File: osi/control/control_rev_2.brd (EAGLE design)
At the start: 25.4 x 25.4 mm, 15 parts, among them U1 ATMEGA168, Y1 RESONATORSMD

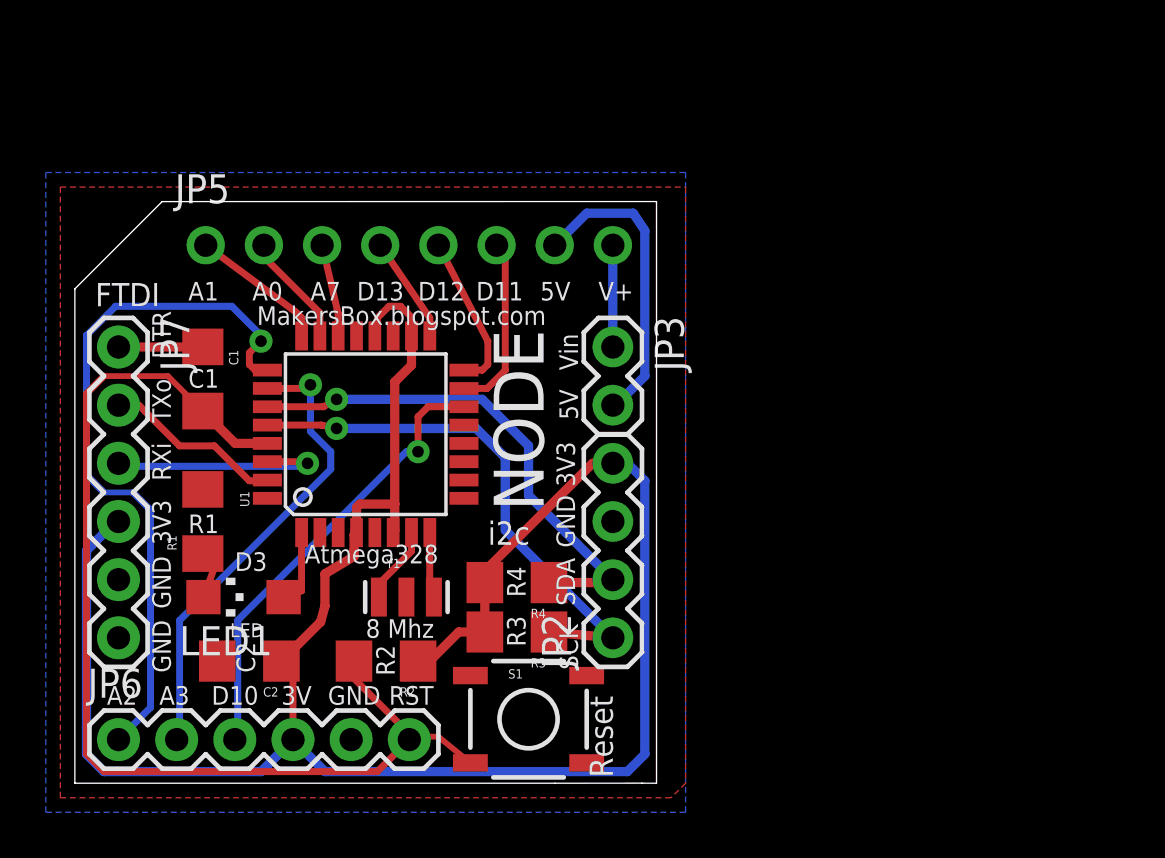
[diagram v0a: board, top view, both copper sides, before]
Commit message: 328p surface mount
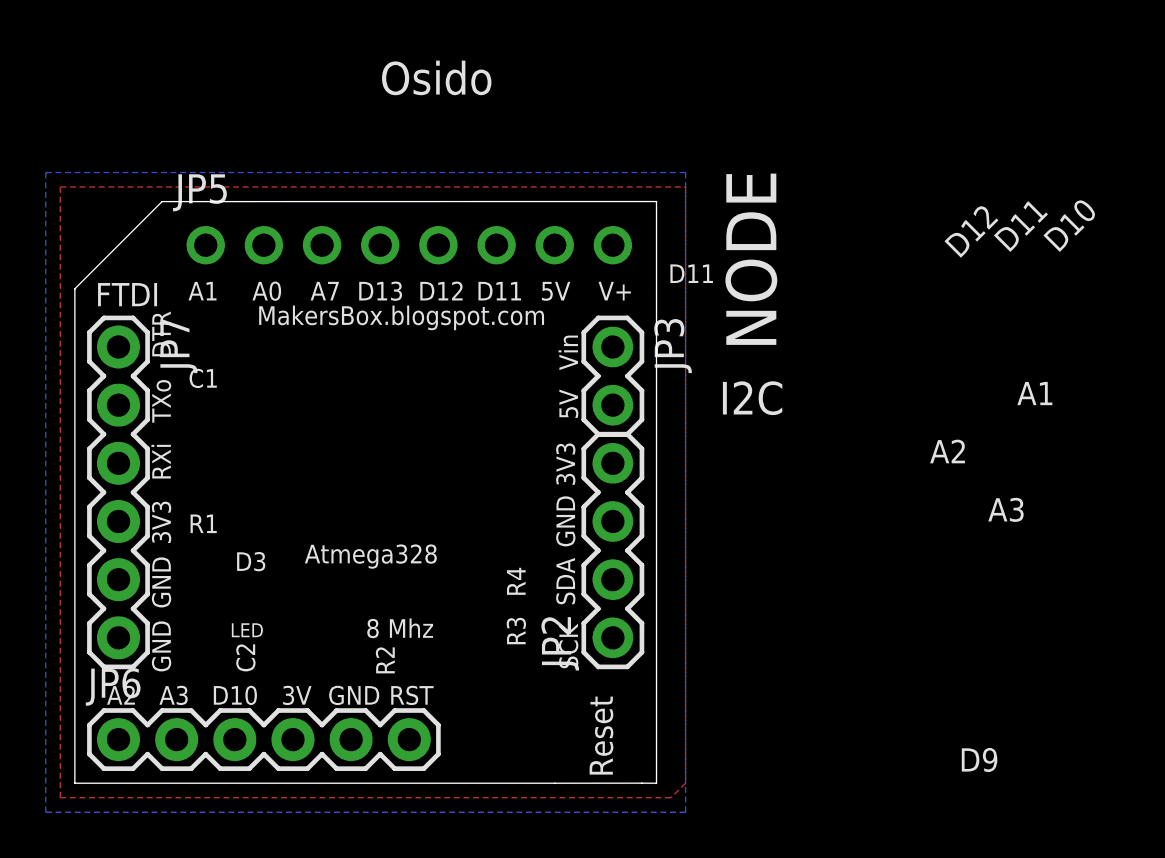
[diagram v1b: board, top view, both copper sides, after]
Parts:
- removed C1, C2, R1, R2, R3, R4: (no value), SparkFun:1206
- removed LED1: (no value), adafruit:CHIPLED_1206
- removed S1: (no value), SparkFun:TACTILE_SWITCH_SMD
- removed U1: ATMEGA168, SparkFun:TQFP32-08
- removed Y1: RESONATORSMD, SparkFun:RESONATOR-SMD
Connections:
- removed net A0: JP5.2, U1.23
- removed net A1: JP5.1, U1.24
- removed net A6: U1.19
- removed net D2: U1.32
- removed net D3: LED1.A, U1.1
- removed net D4: U1.2
- removed net D5: U1.9
- removed net D6: U1.10
- removed net D7: U1.11
- removed net D8: U1.12
- removed net D9: U1.13
- removed net N$1: U1.8, Y1.3
- removed net N$3: U1.7, Y1.1
- removed net N$4: LED1.C, R1.1
- net +3V3: no longer C2.1, R2.1, R3.2, R4.2, U1.18, U1.20, U1.4, U1.6
- net A2: no longer U1.25
- net A3: no longer U1.26
- net A7: no longer U1.22
- net D10: no longer U1.14
- net D11: no longer U1.15
- net D12: no longer U1.16
- net D13: no longer U1.17
- net DTR: no longer C1.1
- net GND: no longer C2.2, R1.2, S1.2, U1.21, U1.3, U1.5, Y1.2
- net RESET: no longer C1.2, R2.2, S1.3, U1.29
- net RXI: no longer U1.30
- net SCL_A5: no longer R3.1, U1.28
- net SDA_A4: no longer R4.1, U1.27
- net TXO: no longer U1.31
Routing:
- net +3V3: track 92.1 -> 0.00 mm
- net RESET: track 47.1 -> 0.00 mm
- net A2: track 31.2 -> 0.00 mm, vias 1 -> 0
- net SCL_A5: track 23.6 -> 0.00 mm, vias 1 -> 0
- net SDA_A4: track 22.5 -> 0.00 mm, vias 1 -> 0
- net A3: track 20.6 -> 0.00 mm, vias 1 -> 0
- net D10: track 19.9 -> 0.00 mm, vias 1 -> 0
- net +5V: track 13.2 -> 0.00 mm
- net RXI: track 10.2 -> 0.00 mm, vias 1 -> 0
- net TXO: track 7.88 -> 0.00 mm
- net D11: track 7.75 -> 0.00 mm
- net D12: track 6.87 -> 0.00 mm
- net A1: track 6.05 -> 0.00 mm
- net A0: track 4.98 -> 0.00 mm
- net D13: track 4.63 -> 0.00 mm
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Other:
- board text added: "A4"
- board text added: "D9"
- board text added: "I2C"
- board text added: "Osido"
- board text removed: "i2c"
